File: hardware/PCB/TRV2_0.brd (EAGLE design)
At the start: 46 x 70 mm, 56 parts, among them IC1 TMP112, IC2 SHT21, IC4 CNY70, IC5 ATMEGA8-AU, Q1 FC-12M, U1 DRV8850_RGY_24

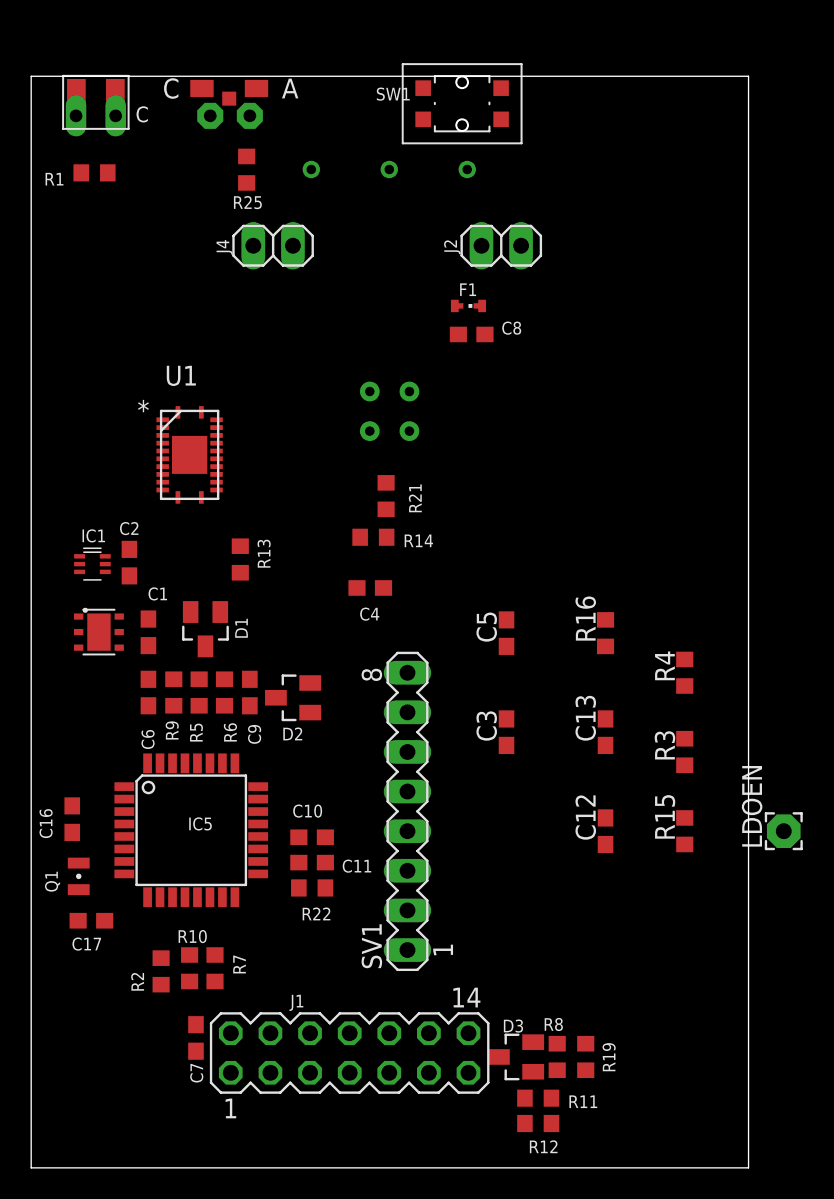
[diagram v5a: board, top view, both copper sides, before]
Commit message: png's updated and motordriver placed on board
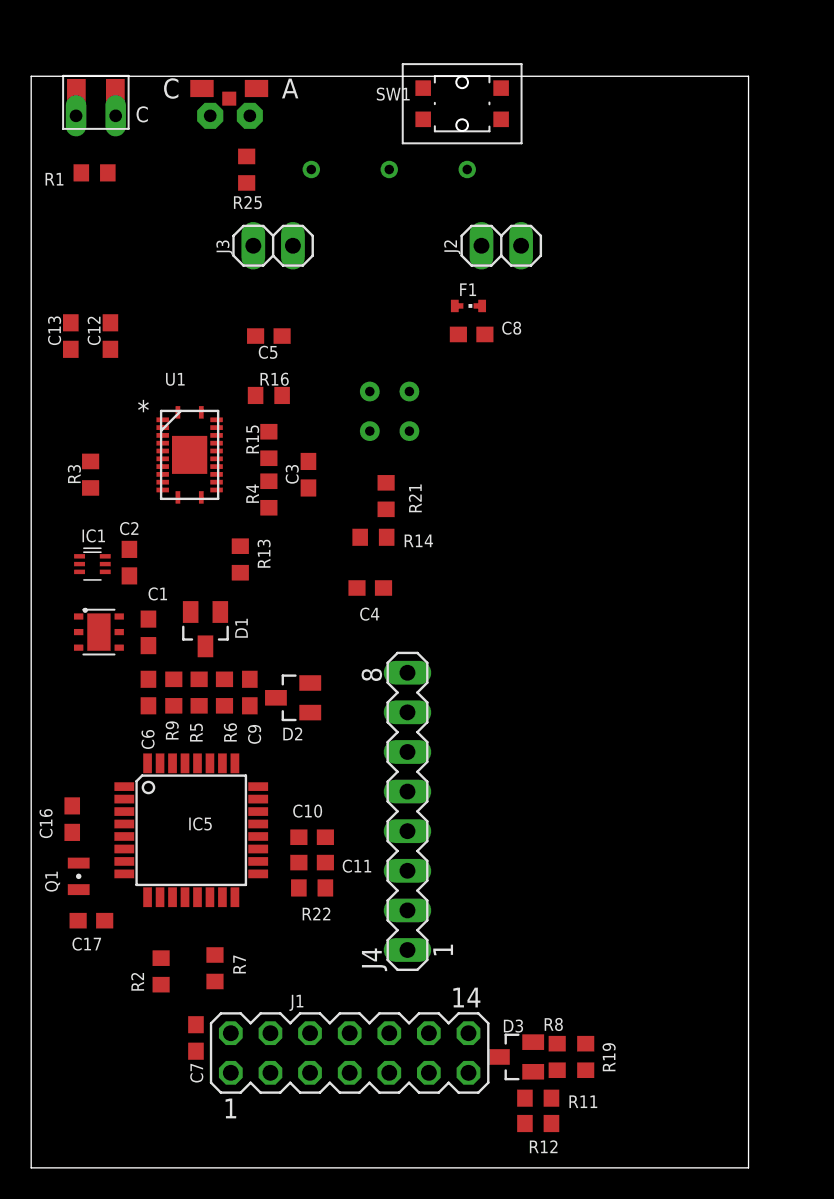
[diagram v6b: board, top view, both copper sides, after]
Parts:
- removed LDOEN: WIREPAD2,15/1,0, wirepad:2,15/1,0
- removed R10: 4K7, resistor:R0603
- removed SV1: (no value), con-lstb:MA08-1
- added J3: (no value), pinhead:1X02
- J4: device pinhead:1X02 -> con-lstb:MA08-1
- moved C12 44.9 mm to (5.08, 53.3)
- moved C13 42.7 mm to (2.54, 53.3)
- moved R3 42.0 mm to (3.81, 44.5)
- moved J4 37.3 mm to (24.1, 22.9), turned to 90 degrees
- moved R15 36.4 mm to (15.2, 46.4)
- moved R4 29.0 mm to (15.2, 43.2)
- moved R16 26.4 mm to (15.2, 49.5), turned to 0 degrees
- moved C5 24.4 mm to (15.2, 53.3), turned to 180 degrees
- moved C3 20.8 mm to (17.8, 44.5)
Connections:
- removed net A1: R16.2, U1.16
- removed net BOILER: IC5.10
- removed net D3: U1.5
- removed net D5: U1.7
- removed net D6: U1.6
- removed net D7: U1.8
- removed net ML: IC5.25
- removed net MR: IC5.26
- removed net N$16: LDOEN.1, U1.10
- removed net N$3: R10.1, SV1.2
- removed net VCC1: C12.2, C13.2, C5.1, U1.18, U1.19, U1.20
- net ANT: now also J4.8; no longer SV1.8
- net GND: now also J4.7; no longer SV1.7
- net MC: now also IC5.19, R16.2, U1.16; no longer IC5.22
- net MI: no longer IC5.19
- net N$11: now also J3.1; no longer J4.1
- net N$2: now also J3.2; no longer J4.2
- net RFMIRQ: now also J4.2; no longer R10.2
- net RFVCC: now also J4.1; no longer SV1.1
- net SPI_MISO: now also J4.6; no longer SV1.6
- net SPI_MOSI: now also J4.5; no longer SV1.5
- net SPI_NNS: now also J4.3; no longer SV1.3
- net SPI_SCLK: now also J4.4; no longer SV1.4
- net VCC: now also C12.2, C13.2, C5.1, U1.18, U1.19, U1.20

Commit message: changes as pr deniz requests
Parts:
- removed C3: 2.2uF, resistor:C0603
- removed R15: 1K, resistor:R0603
- removed R4: 3K, resistor:R0603
- IC2: value SHT21 -> IC2
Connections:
- removed net N$14: R15.2, R4.1, U1.14
- removed net N$15: C3.1, R4.2, U1.15
- net GND: no longer C3.2, R15.1
- net MC: no longer IC4.C, IC5.19, R14.1
- net MI: now also IC4.C, IC5.19, R14.1
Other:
- board text added: "IC2"

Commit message: Motor driver conncedted
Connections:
- new net ML: IC5.25, U1.5, U1.8
- new net MR: IC5.26, U1.6, U1.7
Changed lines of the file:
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@@
 <wire x1="11.8874" y1="44.97" x2="14.39" y2="53.34" width="0" layer="19" extent="1-1"/>
+</signal>
+<signal name="ML">
+<contactref element="U1" pad="5"/>
+<contactref element="U1" pad="8"/>
+<contactref element="IC5" pad="25"/>
+<wire x1="8.4326" y1="44.97" x2="8.4326" y2="46.47" width="0" layer="19" extent="1-1"/>
+<wire x1="13.06360625" y1="25.941603125" x2="8.4326" y2="44.97" width="0" layer="19" extent="1-1"/>
+</signal>
+<signal name="MR">
+<contactref element="U1" pad="6"/>
+<contactref element="U1" pad="7"/>
+<contactref element="IC5" pad="26"/>
+<wire x1="8.4326" y1="45.47" x2="8.4326" y2="45.97" width="0" layer="19" extent="1-1"/>
+<wire x1="12.26360625" y1="25.941603125" x2="8.4326" y2="45.47" width="0" layer="19" extent="1-1"/>
 </signal>
 </signals>
